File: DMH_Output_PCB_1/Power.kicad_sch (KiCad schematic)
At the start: 14 parts, among them J0 Conn_01x01, J100 IDC_02x05, J101 IDC_02x08

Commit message: Schematic in progress
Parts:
- removed C5: 47uF, Capacitor_THT:CP_Radial_D4.0mm_P1.50mm, symbol Device:C_Polarized
- removed C6: 100nF, Capacitor_THT:C_Disc_D4.3mm_W1.9mm_P5.00mm, symbol Device:C
- removed D3, D4, D5: SB140, Diode_THT:D_DO-41_SOD81_P10.16mm_Horizontal, symbol Diode:SB140
- removed J101: IDC_02x08, SynthStuff:IDC-Header_2x08_P2.54mm_Vertical_Eurorack, symbol SynthStuff:Eurorack_Power_Connector_16Pin
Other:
- note removed: "Delete what's not needed!"

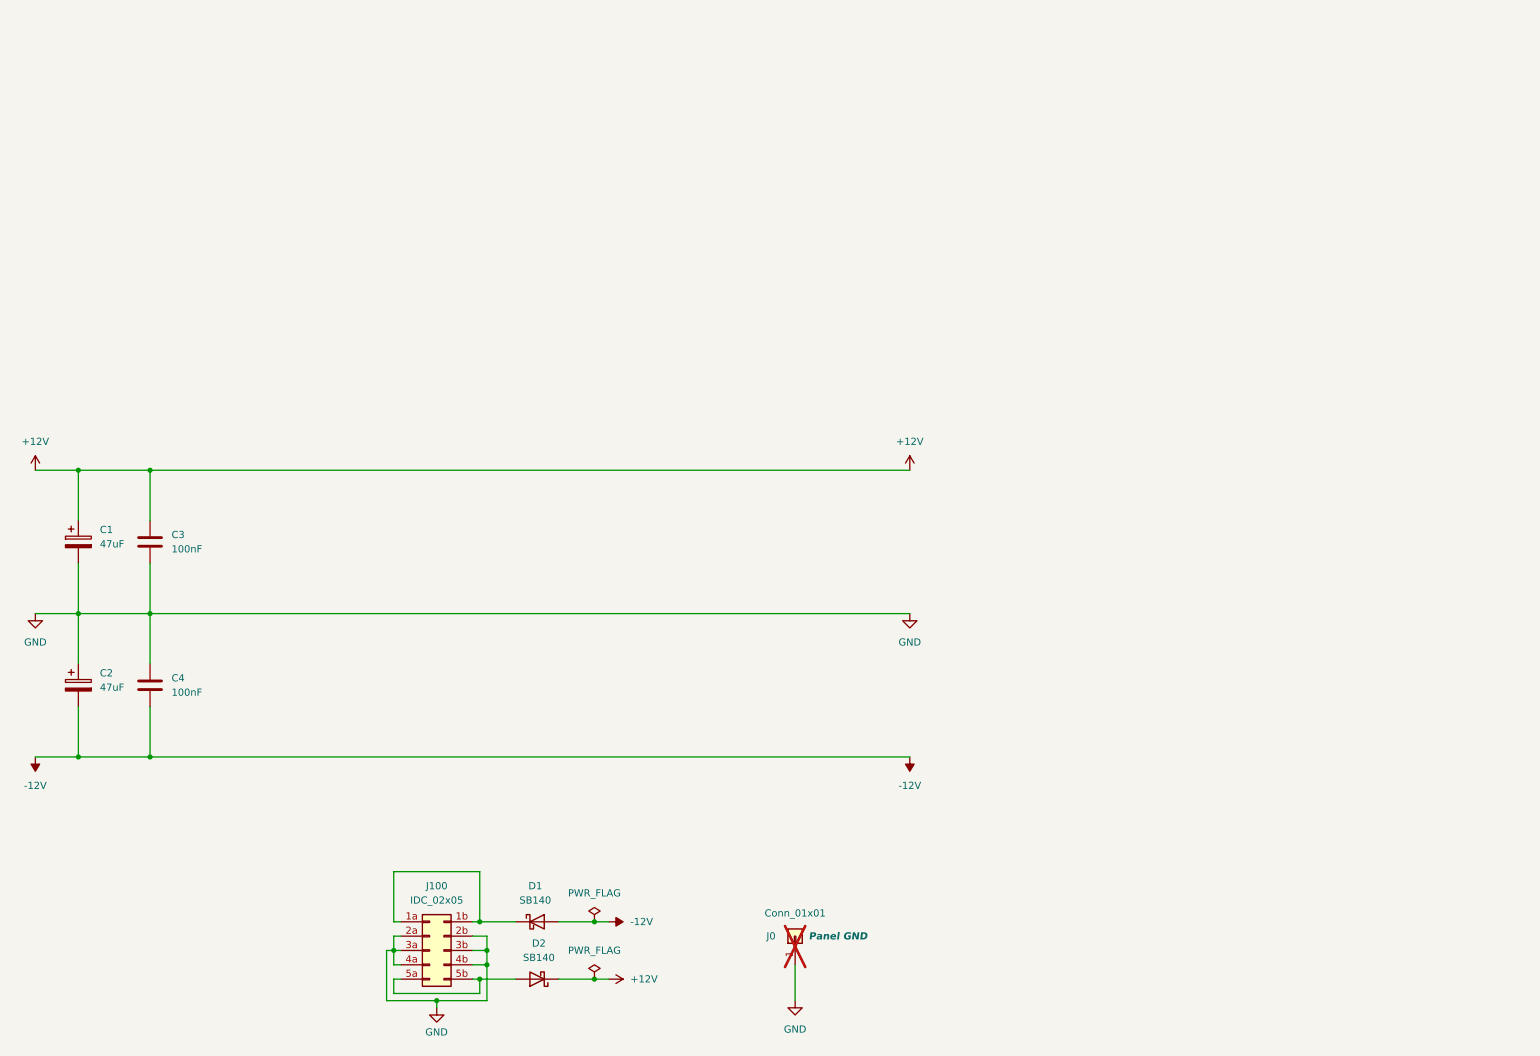
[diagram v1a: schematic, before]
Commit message: Updated meters resistor values
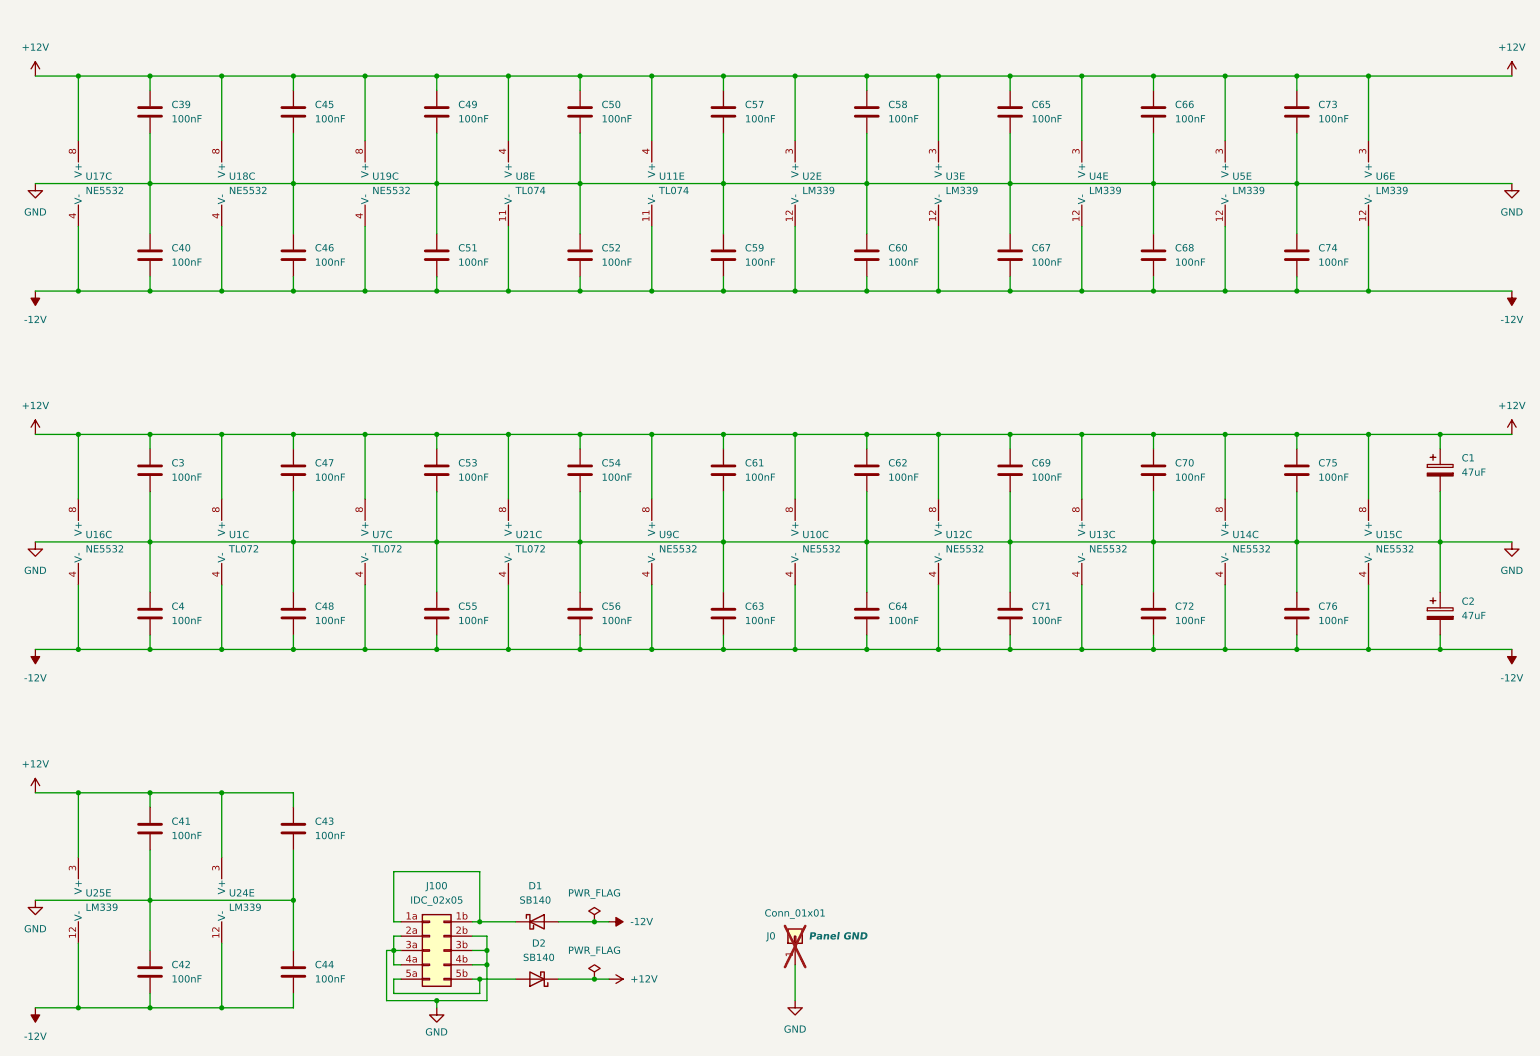
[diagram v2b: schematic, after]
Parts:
- added C39, C40, C41, C42, C43, C44, C45, C46, C47, C48, C49, C50, C51, C52, C53, C54, C55, C56, C57, C58, C59, C60, C61, C62, C63, C64, C65, C66, C67, C68, C69, C70, C71, C72, C73, C74, C75, C76: 100nF, Capacitor_THT:C_Disc_D4.3mm_W1.9mm_P5.00mm, symbol Device:C
- added U1, U21, U7: TL072, Package_DIP:DIP-8_W7.62mm_Socket, symbol Amplifier_Operational:TL072
- added U10, U12, U13, U14, U15, U16, U17, U18, U19, U9: NE5532, Package_DIP:DIP-8_W7.62mm_Socket, symbol Amplifier_Operational:NE5532
- added U11, U8: TL074, Package_DIP:DIP-14_W7.62mm_Socket, symbol Amplifier_Operational:TL074
- added U2, U24, U25, U3, U4, U5, U6: LM339, Package_DIP:DIP-14_W7.62mm_Socket, symbol Comparator:LM339
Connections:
- net +12V: now also C39.1, C41.1, C43.1, C45.1, C47.1, C49.1, C50.1, C53.1, C54.1, C57.1, C58.1, C61.1, C62.1, C65.1, C66.1, C69.1, C70.1, C73.1, C75.1, U1.8 (V+), U10.8 (V+), U11.4 (V+), U12.8 (V+), U13.8 (V+), U14.8 (V+), U15.8 (V+), U16.8 (V+), U17.8 (V+), U18.8 (V+), U19.8 (V+), U2.3 (V+), U21.8 (V+), U24.3 (V+), U25.3 (V+), U3.3 (V+), U4.3 (V+), U5.3 (V+), U6.3 (V+), U7.8 (V+), U8.4 (V+), U9.8 (V+)
- net -12V: now also C40.2, C42.2, C44.2, C46.2, C48.2, C51.2, C52.2, C55.2, C56.2, C59.2, C60.2, C63.2, C64.2, C67.2, C68.2, C71.2, C72.2, C74.2, C76.2, U1.4 (V-), U10.4 (V-), U11.11 (V-), U12.4 (V-), U13.4 (V-), U14.4 (V-), U15.4 (V-), U16.4 (V-), U17.4 (V-), U18.4 (V-), U19.4 (V-), U2.12 (V-), U21.4 (V-), U24.12 (V-), U25.12 (V-), U3.12 (V-), U4.12 (V-), U5.12 (V-), U6.12 (V-), U7.4 (V-), U8.11 (V-), U9.4 (V-)
- net GND: now also C39.2, C40.1, C41.2, C42.1, C43.2, C44.1, C45.2, C46.1, C47.2, C48.1, C49.2, C50.2, C51.1, C52.1, C53.2, C54.2, C55.1, C56.1, C57.2, C58.2, C59.1, C60.1, C61.2, C62.2, C63.1, C64.1, C65.2, C66.2, C67.1, C68.1, C69.2, C70.2, C71.1, C72.1, C73.2, C74.1, C75.2, C76.1
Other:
- moved on the sheet: C1, C2, C3, C4

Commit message: Adjustments during breadboarding
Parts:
- removed U21: TL072, Package_DIP:DIP-8_W7.62mm_Socket, symbol Amplifier_Operational:TL072
- added U20: TL072, Package_DIP:DIP-8_W7.62mm_Socket, symbol Amplifier_Operational:TL072
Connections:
- net +12V: now also U20.8 (V+)
- net -12V: now also U20.4 (V-)
